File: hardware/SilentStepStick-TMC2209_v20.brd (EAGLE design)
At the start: 15.2 x 20.3 mm, 25 parts, among them IC2 TMC2209-LA, J1 MA08-1, J2 MA08-1, J3 MA02-1, X1 PASSER-04, X2 PASSER-04

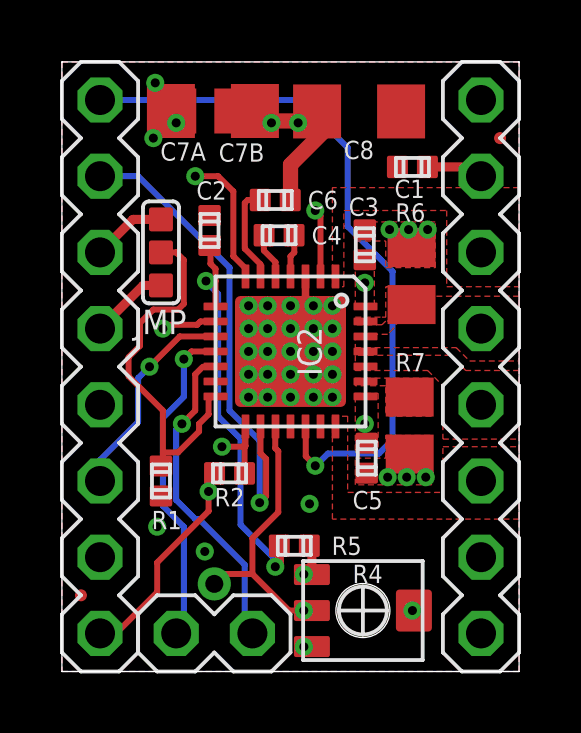
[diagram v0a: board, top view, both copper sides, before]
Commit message: updated schematics
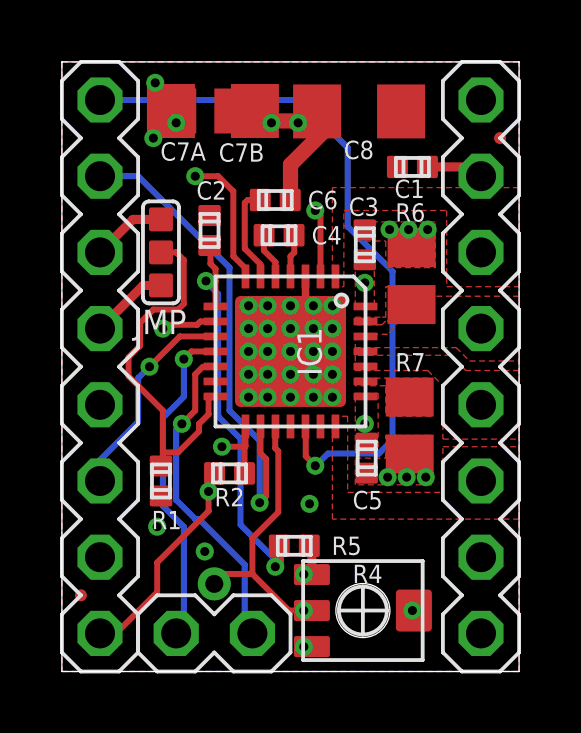
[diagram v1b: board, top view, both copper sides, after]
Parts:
- renumbered IC2 to IC1
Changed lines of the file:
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@@
 <attribute name="VALUE" x="6.6205" y="20.271" size="0.6096" layer="27" rot="R180"/>
 </element>
-<element name="IC2" library="we-chip" package="QFN28-PAD3.7" value="TMC2209-LA" x="7.62" y="10.668" smashed="yes" rot="R270">
+<element name="IC1" library="we-chip" package="QFN28-PAD3.7" value="TMC2209-LA" x="7.62" y="10.668" smashed="yes" rot="R270">
 <attribute name="NAME" x="8.255" y="10.668" size="0.8128" layer="25" font="vector" ratio="10" rot="R270" align="center"/>
 <attribute name="VALUE" x="6.985" y="10.668" size="0.8128" layer="27" font="vector" ratio="10" rot="R270" align="center"/>
@@
 <contactref element="J3" pad="2"/>
 <wire x1="4.064" y1="1.524" x2="3.81" y2="1.27" width="0.2" layer="16"/>
-<contactref element="IC2" pad="11"/>
+<contactref element="IC1" pad="11"/>
 <wire x1="4.064" y1="10.414" x2="4.064" y2="9.1567" width="0.2" layer="16"/>
 <wire x1="4.064" y1="9.1567" x2="3.3655" y2="8.4582" width="0.2" layer="16"/>
@@
 <contactref element="J3" pad="1"/>
 <wire x1="6.096" y1="1.524" x2="6.35" y2="1.27" width="0.2" layer="16"/>
-<contactref element="IC2" pad="12"/>
+<contactref element="IC1" pad="12"/>
 <wire x1="4.699" y1="10.16" x2="4.445" y2="9.906" width="0.2" layer="1"/>
 <wire x1="4.445" y1="9.906" x2="4.445" y2="8.6995" width="0.2" layer="1"/>
@@
 <wire x1="6.5913" y1="5.6261" x2="6.5913" y2="7.6962" width="0.2" layer="16"/>
 <wire x1="6.5913" y1="7.6962" x2="5.588" y2="8.6995" width="0.2" layer="16"/>
-<contactref element="IC2" pad="16"/>
+<contactref element="IC1" pad="16"/>
 <contactref element="J1" pad="2"/>
 </signal>
@@
 <wire x1="10.5664" y1="7.2644" x2="11.0236" y2="7.7216" width="0.2" layer="16"/>
 <wire x1="11.0236" y1="7.7216" x2="11.0236" y2="13.335" width="0.2" layer="16"/>
-<contactref element="IC2" pad="19"/>
+<contactref element="IC1" pad="19"/>
 <contactref element="J1" pad="1"/>
 </signal>
@@
 <contactref element="J2" pad="1"/>
 <contactref element="C7B" pad="1"/>
-<contactref element="IC2" pad="28"/>
-<contactref element="IC2" pad="22"/>
+<contactref element="IC1" pad="28"/>
+<contactref element="IC1" pad="22"/>
 <contactref element="C8" pad="1"/>
 <via x="6.985" y="18.288" extent="1-16" drill="0.3"/>
@@
 <contactref element="J2" pad="8"/>
 <contactref element="C7B" pad="2"/>
-<contactref element="IC2" pad="18"/>
-<contactref element="IC2" pad="TP"/>
-<contactref element="IC2" pad="3"/>
-<contactref element="IC2" pad="20"/>
-<contactref element="IC2" pad="13"/>
+<contactref element="IC1" pad="18"/>
+<contactref element="IC1" pad="TP"/>
+<contactref element="IC1" pad="3"/>
+<contactref element="IC1" pad="20"/>
+<contactref element="IC1" pad="13"/>
 <via x="4.7625" y="4.0005" extent="1-16" drill="0.3"/>
 <via x="3.048" y="17.78" extent="1-16" drill="0.3"/>
@@
 </polygon>
 <contactref element="J2" pad="4"/>
-<contactref element="IC2" pad="24"/>
+<contactref element="IC1" pad="24"/>
 </signal>
 <signal name="OA2">
@@
 </polygon>
 <contactref element="J2" pad="3"/>
-<contactref element="IC2" pad="21"/>
+<contactref element="IC1" pad="21"/>
 </signal>
 <signal name="OB2">
@@
 </polygon>
 <contactref element="J2" pad="6"/>
-<contactref element="IC2" pad="1"/>
+<contactref element="IC1" pad="1"/>
 </signal>
 <signal name="OB1">
@@
 </polygon>
 <contactref element="J2" pad="5"/>
-<contactref element="IC2" pad="26"/>
+<contactref element="IC1" pad="26"/>
 </signal>
 <signal name="VIO">
@@
 <wire x1="6.088" y1="7.485" x2="6.096" y2="7.493" width="0.2" layer="1"/>
 <contactref element="J2" pad="7"/>
-<contactref element="IC2" pad="15"/>
+<contactref element="IC1" pad="15"/>
 <wire x1="12.184" y1="16.819" x2="13.661" y2="16.819" width="0.3048" layer="1"/>
 <wire x1="13.661" y1="16.819" x2="13.97" y2="16.51" width="0.3048" layer="1"/>
@@
 <wire x1="6.19125" y1="15.71625" x2="6.096" y2="15.621" width="0.2" layer="1"/>
 <wire x1="6.096" y1="15.621" x2="6.096" y2="14.097" width="0.2" layer="1"/>
-<contactref element="IC2" pad="6"/>
+<contactref element="IC1" pad="6"/>
 </signal>
 <signal name="CPI">
@@
 <wire x1="6.731" y1="14.0335" x2="6.731" y2="14.5335" width="0.2" layer="1"/>
 <wire x1="6.731" y1="14.5335" x2="6.739" y2="14.5415" width="0.2" layer="1"/>
-<contactref element="IC2" pad="5"/>
+<contactref element="IC1" pad="5"/>
 </signal>
 <signal name="CPO">
@@
 <wire x1="7.747" y1="13.97" x2="7.747" y2="14.5335" width="0.2" layer="1"/>
 <wire x1="7.747" y1="14.5335" x2="7.739" y2="14.5415" width="0.2" layer="1"/>
-<contactref element="IC2" pad="4"/>
+<contactref element="IC1" pad="4"/>
 </signal>
 <signal name="BRA">
@@
 <vertex x="9.779" y="9.525"/>
 </polygon>
-<contactref element="IC2" pad="23"/>
+<contactref element="IC1" pad="23"/>
 </signal>
 <signal name="BRB">
@@
 <vertex x="9.779" y="11.557"/>
 </polygon>
-<contactref element="IC2" pad="27"/>
+<contactref element="IC1" pad="27"/>
 </signal>
 <signal name="+5V">
@@
 <wire x1="5.9563" y1="4.8895" x2="5.9563" y2="7.7597" width="0.2" layer="16"/>
 <wire x1="5.9563" y1="7.7597" x2="5.207" y2="8.509" width="0.2" layer="16"/>
-<contactref element="IC2" pad="8"/>
+<contactref element="IC1" pad="8"/>
 </signal>
 <signal name="VREF">
@@
 <wire x1="6.35" y1="3.2512" x2="5.4102" y2="3.2512" width="0.2" layer="1"/>
 <wire x1="5.4102" y1="3.2512" x2="5.08" y2="2.921" width="0.2" layer="1"/>
-<contactref element="IC2" pad="17"/>
+<contactref element="IC1" pad="17"/>
 </signal>
 <signal name="MS1">
 <via x="3.3655" y="11.43" extent="1-16" drill="0.3"/>
-<contactref element="IC2" pad="9"/>
+<contactref element="IC1" pad="9"/>
 <contactref element="J1" pad="7"/>
 <wire x1="3.3655" y1="11.43" x2="3.4925" y2="11.303" width="0.2" layer="15"/>
@@
 <via x="2.921" y="10.16" extent="1-16" drill="0.3"/>
 <wire x1="2.921" y1="10.16" x2="2.54" y2="9.779" width="0.2" layer="16"/>
-<contactref element="IC2" pad="10"/>
+<contactref element="IC1" pad="10"/>
 <contactref element="J1" pad="6"/>
 <wire x1="1.27" y1="6.35" x2="1.27" y2="7.0485" width="0.2" layer="16"/>
@@
 <contactref element="JMP" pad="2"/>
 <wire x1="5.1435" y1="9.1445" x2="5.12" y2="9.168" width="0.2" layer="1"/>
-<contactref element="IC2" pad="14"/>
+<contactref element="IC1" pad="14"/>
 <wire x1="3.3655" y1="6.9135" x2="3.302" y2="6.85" width="0.2" layer="1"/>
 <wire x1="3.3655" y1="6.9135" x2="3.3655" y2="7.3025" width="0.2" layer="1"/>
@@
 <wire x1="1.8034" y1="1.27" x2="3.175" y2="2.6416" width="0.2" layer="1"/>
 <wire x1="3.175" y1="2.6416" x2="3.175" y2="3.6322" width="0.2" layer="1"/>
-<contactref element="IC2" pad="2"/>
+<contactref element="IC1" pad="2"/>
 <contactref element="J1" pad="8"/>
 <wire x1="4.8895" y1="6.00075" x2="4.8895" y2="6.4055" width="0.2" layer="1"/>
@@
 </signal>
 <signal name="SPREAD">
-<contactref element="IC2" pad="7"/>
+<contactref element="IC1" pad="7"/>
 <contactref element="J1" pad="5"/>
 <wire x1="6.12" y1="13.168" x2="6.12" y2="13.438" width="0.2" layer="1"/>
